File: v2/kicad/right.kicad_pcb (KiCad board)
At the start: 2 copper layers, 158.5 x 120.3 mm, 70 parts

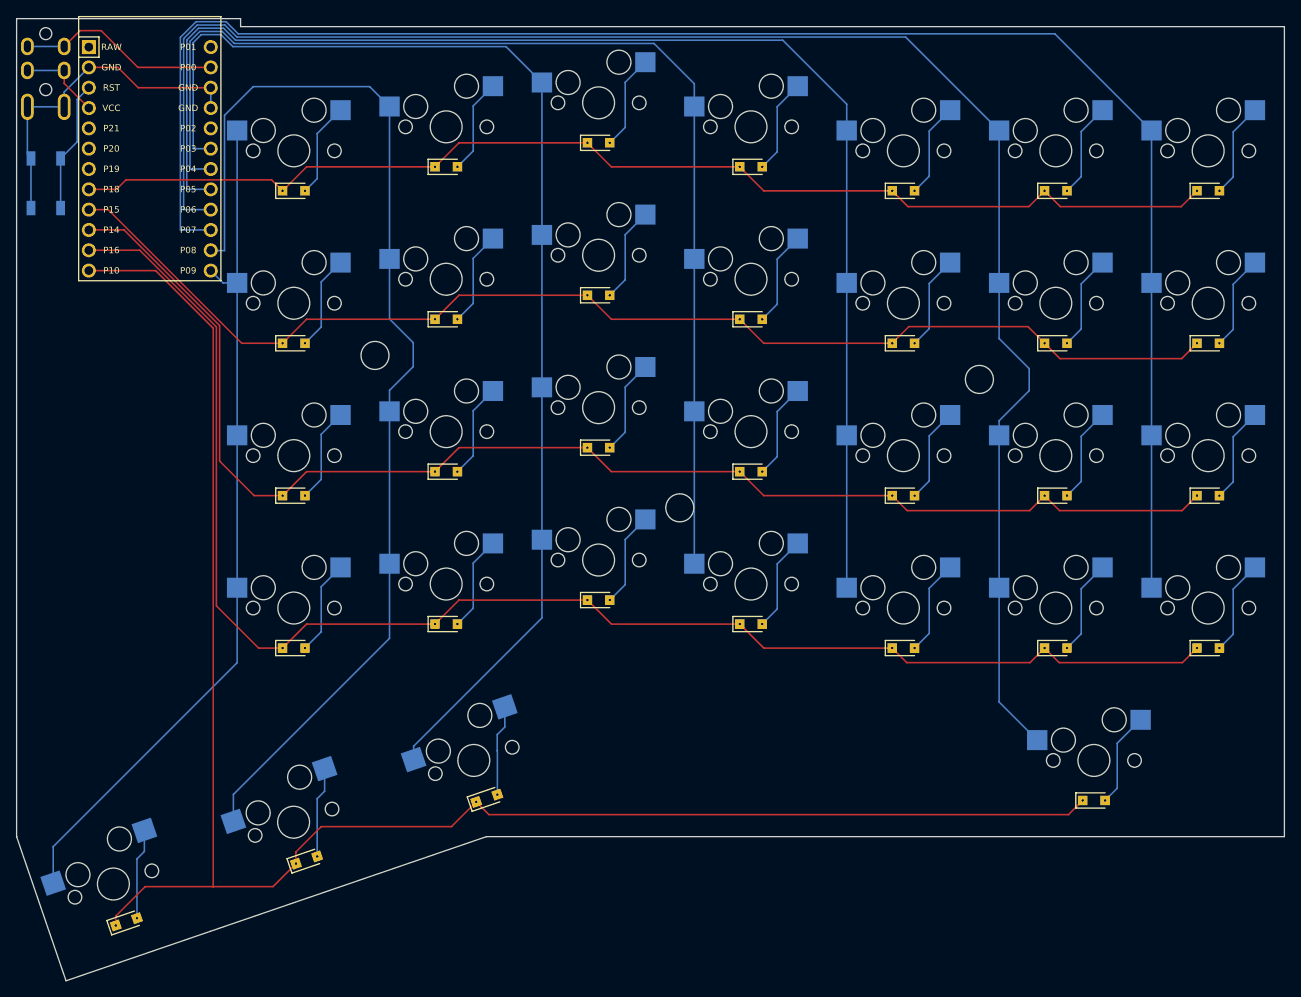
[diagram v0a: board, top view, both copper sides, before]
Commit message: Move backspace 1u to the left
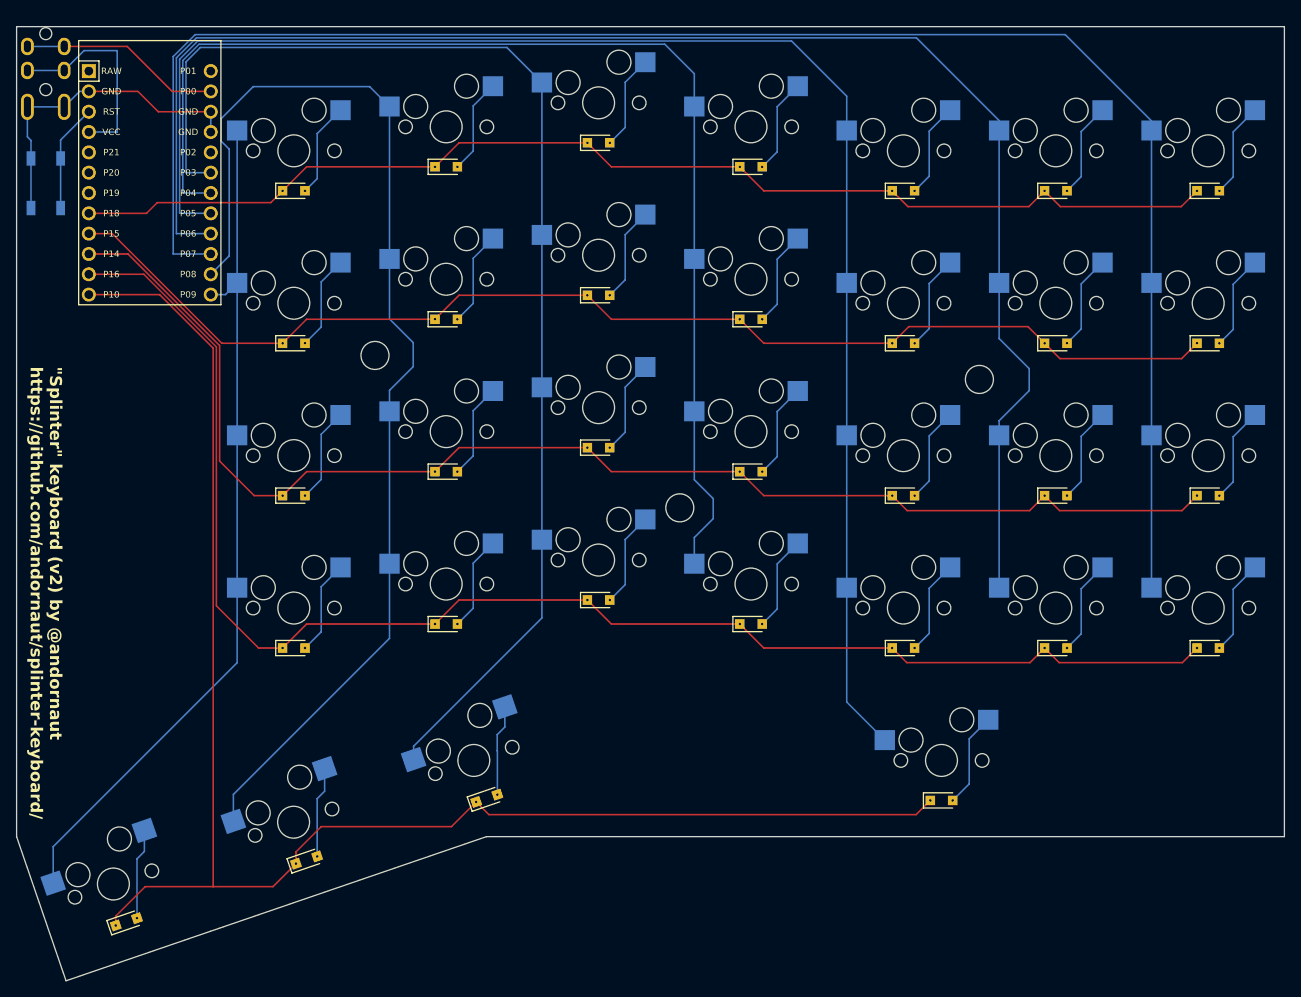
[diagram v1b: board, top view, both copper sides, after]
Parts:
- moved D17 83.2 mm to (340.0, 196.7)
- moved S17 83.2 mm to (340.0, 191.7)
- moved D21 79.8 mm to (335.3, 120.5)
- moved S21 79.8 mm to (335.3, 115.5)
- moved D18 78.5 mm to (335.3, 177.7)
- moved D19 78.5 mm to (335.3, 158.6)
- moved D20 78.5 mm to (335.3, 139.6)
- moved S18 78.5 mm to (335.3, 172.7)
- moved S19 78.5 mm to (335.3, 153.6)
- moved S20 78.5 mm to (335.3, 134.6)
- moved D10 19.3 mm to (278.1, 155.6)
- moved D11 19.3 mm to (278.1, 136.6)
- moved D12 19.3 mm to (278.1, 117.5)
- moved D13 19.3 mm to (259.1, 177.7)
- moved D14 19.3 mm to (259.1, 158.6)
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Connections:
- net dash_meta renamed zero_number
- D1 pad 2: mirror_one_bottom -> mirror_two_bottom
- D10 pad 2: mirror_three_home -> mirror_four_home
- D11 pad 2: mirror_three_top -> mirror_four_top
- D12 pad 2: mirror_three_number -> mirror_four_number
- D13 pad 2: mirror_four_bottom -> mirror_five_bottom
- D14 pad 2: mirror_four_home -> mirror_five_home
- D15 pad 2: mirror_four_top -> mirror_five_top
- D16 pad 2: mirror_four_number -> mirror_five_number
- D17 pad 1: P16 -> P10
- D17 pad 2: mirror_five_bottom -> zero_meta
- D18 pad 1: P14 -> P16
- D18 pad 2: mirror_five_home -> zero_bottom
- D19 pad 1: P15 -> P14
- D19 pad 2: mirror_five_top -> zero_home
- D2 pad 2: mirror_one_home -> mirror_two_home
- D20 pad 1: P18 -> P15
- D20 pad 2: mirror_five_number -> zero_top
- D21 pad 1: P10 -> P18
- D3 pad 2: mirror_one_top -> mirror_two_top
- D4 pad 2: mirror_one_number -> mirror_two_number
- D5 pad 2: mirror_two_bottom -> mirror_three_bottom
- D6 pad 2: mirror_two_home -> mirror_three_home
- D7 pad 2: mirror_two_top -> mirror_three_top
- D8 pad 2: mirror_two_number -> mirror_three_number
- D9 pad 2: mirror_three_bottom -> mirror_four_bottom
- S1 pad 1: P5 -> P4
- S1 pad 2: mirror_one_bottom -> mirror_two_bottom
- S10 pad 1: P3 -> P8
- S10 pad 2: mirror_three_home -> mirror_four_home
- S11 pad 1: P3 -> P8
- S11 pad 2: mirror_three_top -> mirror_four_top
- S12 pad 1: P3 -> P8
- S12 pad 2: mirror_three_number -> mirror_four_number
- S13 pad 1: P8 -> P9
- S13 pad 2: mirror_four_bottom -> mirror_five_bottom
- S14 pad 1: P8 -> P9
- S14 pad 2: mirror_four_home -> mirror_five_home
- S15 pad 1: P8 -> P9
- S15 pad 2: mirror_four_top -> mirror_five_top
- S16 pad 1: P8 -> P9
- S16 pad 2: mirror_four_number -> mirror_five_number
- S17 pad 1: P9 -> P5
- S17 pad 2: mirror_five_bottom -> zero_meta
- S18 pad 1: P9 -> P5
- S18 pad 2: mirror_five_home -> zero_bottom
- S19 pad 1: P9 -> P5
- S19 pad 2: mirror_five_top -> zero_home
- S2 pad 1: P5 -> P4
- S2 pad 2: mirror_one_home -> mirror_two_home
- S20 pad 1: P9 -> P5
- S20 pad 2: mirror_five_number -> zero_top
- S21 pad 1: P6 -> P5
- S3 pad 1: P5 -> P4
- S3 pad 2: mirror_one_top -> mirror_two_top
- S4 pad 1: P5 -> P4
- S4 pad 2: mirror_one_number -> mirror_two_number
- S5 pad 1: P4 -> P3
- S5 pad 2: mirror_two_bottom -> mirror_three_bottom
- S6 pad 1: P4 -> P3
- S6 pad 2: mirror_two_home -> mirror_three_home
- S7 pad 1: P4 -> P3
- S7 pad 2: mirror_two_top -> mirror_three_top
- S8 pad 1: P4 -> P3
- S8 pad 2: mirror_two_number -> mirror_three_number
- S9 pad 1: P3 -> P8
- S9 pad 2: mirror_three_bottom -> mirror_four_bottom
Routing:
- net P5: track 169.1 -> 192.8 mm
- net P10: track 218.5 -> 196.8 mm
- net P6: track 214.2 -> 195.9 mm
- net VCC: track 10.6 -> 26.0 mm
- net zero_home: track 0.00 -> 11.9 mm
- net zero_bottom: track 0.00 -> 11.9 mm
- net mirror_one_home: track 11.9 -> 0.00 mm
- net mirror_one_bottom: track 11.9 -> 0.00 mm
- net mirror_one_number: track 11.9 -> 0.00 mm
- net zero_top: track 0.00 -> 11.9 mm
- net zero_meta: track 0.00 -> 11.9 mm
- net mirror_one_top: track 11.9 -> 0.00 mm
- net P4: track 144.8 -> 149.5 mm
- net RST: track 16.5 -> 13.5 mm
- net P8: track 141.6 -> 144.4 mm
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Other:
- board size 158.5 x 120.3 mm -> 158.5 x 119.3 mm
- board text added: "Pro Micro ATmega32U4 USB-C (3mm longer)"
- board text added: "Reset Switch"
- board text added: "TRRS"
- board text added: "{dblquote}Splinter{dblquote} keyboard (v2) by @andornaut https://github.com/andornaut/splinter-keyboard/"
